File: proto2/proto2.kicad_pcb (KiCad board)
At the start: 2 copper layers, 166 x 111 mm, 158 parts, among them J1 Output 1, J10 Output 6, J11 Device 4, J2 Main Power, J3 Output 2, J4 Output 3, J5 Device 4, J6 Output 4, J7 Device 4, J8 Output 5, J9 Device 4, SW1 SW_DIP_x04, U1 AQY282SX, U10 AQY282SX, U11 AQY282SX, U12 AQY282SX, U13 AP1117-50, U14 JTD1548S15, U2 AQY282SX, U3 AQY282SX, U4 AQY282SX, U5 AQY282SX, U6 AQY282SX, U7 AQY282SX, U8 AQY282SX, U9 AQY282SX

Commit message: Routed Board.
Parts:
- removed U14: JTD1548S15, Converter_DCDC:Converter_DCDC_XP_POWER_JTDxxxxxxx_THT
- added C43: 1nF 2kV, Capacitor_SMD:C_0805_2012Metric, F.Cu at (192.8, 106.4)
- added C44: 330uF, Capacitor_SMD:C_0805_2012Metric, F.Cu at (198.8, 128.0)
- added C45: 4.7uF, Capacitor_SMD:C_0805_2012Metric, F.Cu at (198.8, 123.2)
- added C46: 4.7uF, Capacitor_SMD:C_0805_2012Metric, F.Cu at (198.8, 109.2)
- added C47: 330uF, Capacitor_SMD:C_0805_2012Metric, F.Cu at (198.8, 113.2)
- added C48: 100uF, Capacitor_SMD:C_0805_2012Metric, F.Cu at (173.5, 83.2)
- added C49: 1nF 2kV, Capacitor_SMD:C_0805_2012Metric, F.Cu at (192.8, 78.8)
- added C50: 0.33uF, Capacitor_SMD:C_0805_2012Metric, F.Cu at (163.3, 80.3)
- added C51: 01.uF, Capacitor_SMD:C_0805_2012Metric, F.Cu at (160.6, 73.1)
- added C52: 0.1uF, Capacitor_SMD:C_1206_3216Metric, F.Cu at (37.0, 142.5)
- added C53: 0.1uF, Capacitor_SMD:C_1206_3216Metric, F.Cu at (211.8, 141.8)
- added F13: 1A, Resistor_SMD:R_1206_3216Metric, F.Cu at (197.8, 133.5)
- added F14: 500mA, Resistor_SMD:R_0805_2012Metric, F.Cu at (43.8, 139.2)
- added F15: 500mA, Resistor_SMD:R_0805_2012Metric, F.Cu at (61.2, 139.2)
- added F16: 500mA, Resistor_SMD:R_0805_2012Metric, F.Cu at (78.8, 139.2)
- added F17: 500mA, Resistor_SMD:R_0805_2012Metric, F.Cu at (96.2, 139.2)
- added J12: Daughter Card, Connector_PinHeader_2.54mm:PinHeader_1x10_P2.54mm_Vertical, F.Cu at (156.4, 58.0)
- added L43: 2.2uH, Inductor_BCR:Murata_LQH32PN2R2NN0L, F.Cu at (197.8, 117.8)
- added PS1: CUI PDQE20, Converter_BCR:CUI_PDQE20, F.Cu at (187.5, 92.5)
- added R19: R Trim Up, Capacitor_SMD:C_0805_2012Metric, F.Cu at (172.8, 88.5)
- added R20: R Trim Down, Capacitor_SMD:C_0805_2012Metric, F.Cu at (172.5, 95.5)
- added R21: 0R, Capacitor_SMD:C_1206_3216Metric, F.Cu at (159.6, 76.6)
- added REF**: NPTH-.125, STD-xxx:NPTH-.125, F.Cu at (165.0, 103.0)
- added REF**: NPTH-.125, STD-xxx:NPTH-.125, F.Cu at (125.0, 103.0)
- added REF**: Langhe_Carrot, BCR_Art:Langhe_Carrot, F.Cu at (202.4, 70.0)
- MH1, MH3: footprint BCR_STD:STD-M6 -> STD-xxx:NPTH-.125
- MH2, MH4: footprint BCR_STD:STD-M6 -> STD-xxx:STD-.125_wide
- R17, R18: value 1M -> 0R
- SW1: footprint Package_SO:SOP-8_6.62x9.15mm_P2.54mm -> Button_Switch_BCR:CUI_DS04-254-2-04BK-SMT
- U13: value AP1117-50 -> LDO
- moved MH2 137.4 mm to (35.2, 158.0)
- moved R18 137.1 mm to (215.2, 141.8)
- moved MH4 116.1 mm to (213.2, 158.0)
- moved R17 115.6 mm to (33.2, 142.5)
- moved MH1 105.8 mm to (35.2, 58.0)
- moved C18 105.6 mm to (43.8, 143.2), turned to 270 degrees
- moved C16 101.8 mm to (50.8, 143.2), turned to 270 degrees
- moved C17 97.4 mm to (47.2, 143.2), turned to 270 degrees
- moved C26 95.2 mm to (61.2, 143.2), turned to 270 degrees
- moved C15 93.6 mm to (54.2, 143.2), turned to 270 degrees
- moved C23 89.4 mm to (71.8, 143.2), turned to 270 degrees
- moved C25 87.2 mm to (64.8, 143.2), turned to 270 degrees
- moved C31 80.7 mm to (89.2, 143.2), turned to 270 degrees
- moved C38 79.4 mm to (191.5, 137.0), turned to 180 degrees
- moved C24 79.3 mm to (68.2, 143.2), turned to 270 degrees
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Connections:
- net VDQ renamed VDQ1
- BB1 pad 8.13: Net-(BB1-Pad8.13) -> OUT_1
- BB1 pad 8.15: Net-(BB1-Pad8.15) -> OUT_2
- BB1 pad 8.17: Net-(BB1-Pad8.17) -> OUT_3
- BB1 pad 8.19: Net-(BB1-Pad8.19) -> OUT_4
- BB1 pad 8.20: OUT_1 -> Net-(BB1-Pad8.20)
- BB1 pad 8.21: Net-(BB1-Pad8.21) -> OUT_5
- BB1 pad 8.22: OUT_2 -> Net-(BB1-Pad8.22)
- BB1 pad 8.23: Net-(BB1-Pad8.23) -> OUT_6
- BB1 pad 8.24: OUT_3 -> Net-(BB1-Pad8.24)
- BB1 pad 8.25: Net-(BB1-Pad8.25) -> OUT_7
- BB1 pad 8.26: OUT_4 -> Net-(BB1-Pad8.26)
- BB1 pad 8.27: Net-(BB1-Pad8.27) -> OUT_8
- BB1 pad 8.28: OUT_5 -> Net-(BB1-Pad8.28)
- BB1 pad 8.29: Net-(BB1-Pad8.29) -> OUT_9
- BB1 pad 8.30: OUT_6 -> Net-(BB1-Pad8.30)
- BB1 pad 8.31: Net-(BB1-Pad8.31) -> OUT_10
- BB1 pad 8.32: OUT_7 -> Net-(BB1-Pad8.32)
- BB1 pad 8.33: Net-(BB1-Pad8.33) -> OUT_11
- BB1 pad 8.34: OUT_8 -> Net-(BB1-Pad8.34)
- BB1 pad 8.35: Net-(BB1-Pad8.35) -> OUT_12
- BB1 pad 8.36: OUT_9 -> GP_4
- BB1 pad 8.40: OUT_10 -> GP_3
- BB1 pad 8.42: Net-(BB1-Pad8.42) -> GP_2
- BB1 pad 8.44: OUT_11 -> GP_1
- BB1 pad 8.46: OUT_12 -> BS_5
- C18 pad 1: +5V -> 5V_1
- C26 pad 1: +5V -> 5V_2
- C34 pad 1: +5V -> 5V_3
- C42 pad 1: +5V -> 5V_4
- D1 pad 2: Earth -> Net-(D1-Pad2)
- D10 pad 2: Earth -> Net-(D10-Pad2)
- D11 pad 2: Earth -> Net-(D11-Pad2)
- D12 pad 2: Earth -> Net-(D12-Pad2)
- D2 pad 2: Earth -> Net-(D2-Pad2)
- D3 pad 2: Earth -> Net-(D3-Pad2)
- D4 pad 2: Earth -> Net-(D4-Pad2)
- D5 pad 2: Earth -> Net-(D5-Pad2)
- D6 pad 2: Earth -> Net-(D6-Pad2)
- D7 pad 2: Earth -> Net-(D7-Pad2)
- D8 pad 2: Earth -> Net-(D8-Pad2)
- D9 pad 2: Earth -> Net-(D9-Pad2)
- F2 pad 1: DQ01_2 -> DQ1_2
- J1 pad 2: Net-(J1-Pad2) -> Net-(D1-Pad2)
- J1 pad 4: Net-(J1-Pad4) -> Net-(D2-Pad2)
- J10 pad 2: Net-(J10-Pad2) -> Net-(D11-Pad2)
- J10 pad 3: Net-(J10-Pad3) -> Net-(D12-Pad1)
- J10 pad 4: Net-(J10-Pad3) -> Net-(D12-Pad2)
- J3 pad 2: Net-(J3-Pad2) -> Net-(D3-Pad2)
- J3 pad 4: Net-(J3-Pad4) -> Net-(D4-Pad2)
- J4 pad 2: Net-(J4-Pad2) -> Net-(D5-Pad2)
- J4 pad 4: Net-(J4-Pad4) -> Net-(D6-Pad2)
- J6 pad 2: Net-(J6-Pad2) -> Net-(D7-Pad2)
- J6 pad 4: Net-(J6-Pad4) -> Net-(D8-Pad2)
- J8 pad 2: Net-(J8-Pad2) -> Net-(D9-Pad2)
- J8 pad 4: Net-(J8-Pad4) -> Net-(D10-Pad2)
- L10 pad 2: Net-(J3-Pad4) -> Net-(D4-Pad2)
- L12 pad 2: Net-(J4-Pad2) -> Net-(D5-Pad2)
- L14 pad 1: +5V -> 5V_1
- L15 pad 2: Net-(J4-Pad4) -> Net-(D6-Pad2)
- L2 pad 2: Net-(J1-Pad2) -> Net-(D1-Pad2)
- L20 pad 2: Net-(J6-Pad2) -> Net-(D7-Pad2)
- L22 pad 2: Net-(J6-Pad4) -> Net-(D8-Pad2)
- L23 pad 1: +5V -> 5V_2
- L28 pad 2: Net-(J8-Pad2) -> Net-(D9-Pad2)
- L30 pad 2: Net-(J8-Pad4) -> Net-(D10-Pad2)
- L31 pad 1: +5V -> 5V_3
- L36 pad 2: Net-(J10-Pad2) -> Net-(D11-Pad2)
- L37 pad 2: Net-(J10-Pad3) -> Net-(D12-Pad1)
- L38 pad 2: Net-(J10-Pad3) -> Net-(D12-Pad2)
- L39 pad 1: +5V -> 5V_4
- L4 pad 2: Net-(J1-Pad4) -> Net-(D2-Pad2)
- L8 pad 2: Net-(J3-Pad2) -> Net-(D3-Pad2)
- R10 pad 2: OUT_10 -> OUT_6
- R11 pad 2: OUT_3 -> OUT_7
- R12 pad 2: OUT_7 -> OUT_8
- R13 pad 2: OUT_11 -> OUT_9
- R14 pad 2: OUT_4 -> OUT_10
- R15 pad 2: OUT_8 -> OUT_11
- R6 pad 2: OUT_5 -> OUT_2
- R7 pad 2: OUT_9 -> OUT_3
- R8 pad 2: OUT_2 -> OUT_4
- R9 pad 2: OUT_6 -> OUT_5
- RP1 pad 11: OUT_3 -> BS_3
- RP1 pad 13: OUT_2 -> BS_2
- RP1 pad 15: OUT_1 -> BS_1
- RP1 pad 24: Net-(RP1-Pad24) -> BS_5
- RP1 pad 29: Net-(RP1-Pad29) -> OUT_4
- RP1 pad 31: BS_1 -> OUT_3
- RP1 pad 33: BS_2 -> OUT_2
- RP1 pad 35: BS_3 -> OUT_1
- RP1 pad 37: BS_4 -> Net-(RP1-Pad37)
- RP1 pad 7: OUT_4 -> BS_4
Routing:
- net +5V: track 0.00 -> 321.4 mm, vias 0 -> 4
- net OUT_12: track 0.00 -> 241.1 mm, vias 0 -> 5
- net OUT_11: track 0.00 -> 232.3 mm, vias 0 -> 5
- net OUT_10: track 0.00 -> 223.0 mm, vias 0 -> 5
- net OUT_9: track 0.00 -> 212.0 mm, vias 0 -> 5
- net OUT_4: track 0.00 -> 204.1 mm, vias 0 -> 4
- net OUT_8: track 0.00 -> 202.0 mm, vias 0 -> 5
- net OUT_3: track 0.00 -> 191.3 mm, vias 0 -> 4
- net OUT_7: track 0.00 -> 190.6 mm, vias 0 -> 5
- net BS_5: track 0.00 -> 185.0 mm, vias 0 -> 4
- net OUT_6: track 0.00 -> 182.0 mm, vias 0 -> 5
- net OUT_2: track 0.00 -> 179.6 mm, vias 0 -> 4
- net OUT_1: track 0.00 -> 172.5 mm, vias 0 -> 4
- net OUT_5: track 0.00 -> 170.6 mm, vias 0 -> 5
- net BS_1: track 0.00 -> 146.0 mm, vias 0 -> 3
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- added copper zone on B.Cu, net Earth
- added copper zone on B.Cu, net GND
- added copper zone on F.Cu, net GNDPWR
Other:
- board size 166 x 111 mm -> 187.5 x 109.8 mm
- board text added: "Langhe Greenhaus ©2021 LNG-PCB-003"

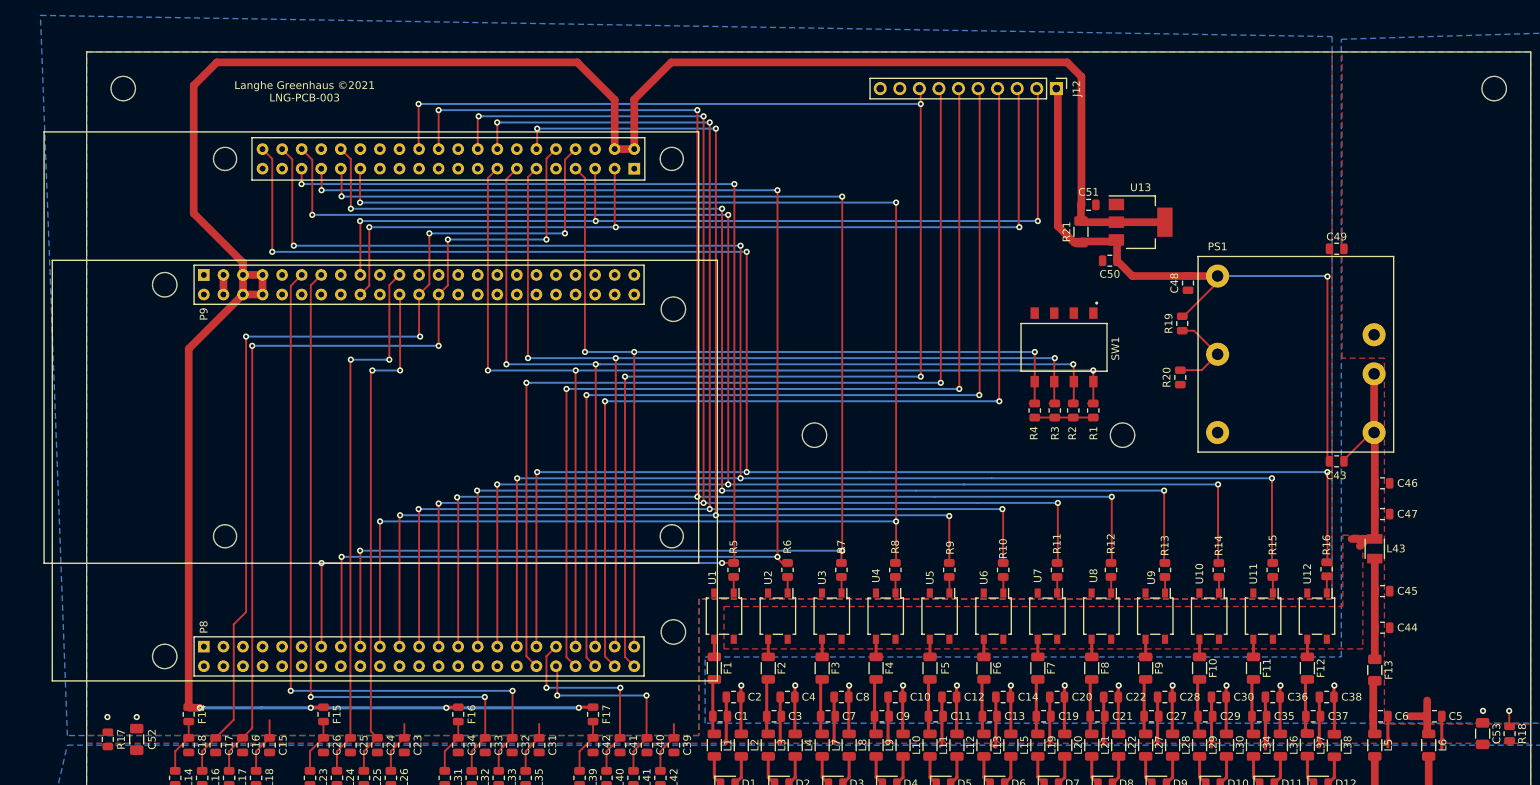
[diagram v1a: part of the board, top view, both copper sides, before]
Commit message: Added correct cap and moved DIP switches.
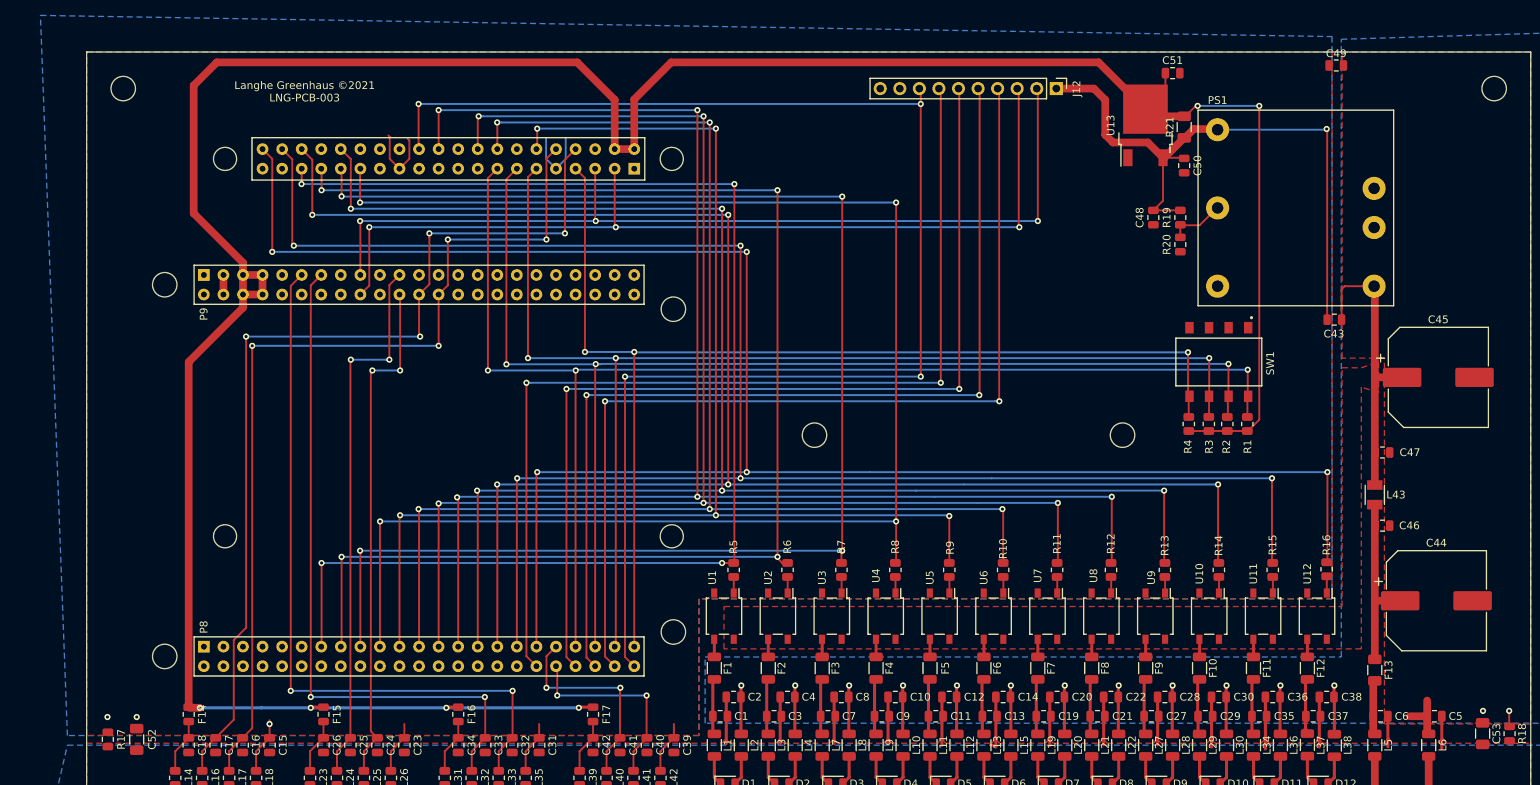
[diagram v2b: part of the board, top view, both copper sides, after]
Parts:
- C44: footprint Capacitor_SMD:C_0805_2012Metric -> Capacitor_BCR:CP_Elec_13x12.5
- C45: value 4.7uF -> 330uF; footprint Capacitor_SMD:C_0805_2012Metric -> Capacitor_BCR:CP_Elec_13x12.5
- C47: value 330uF -> 4.7uF
- U13: footprint Package_TO_SOT_SMD:SOT-223-3_TabPin2 -> JLCPCB:TO-252-2
- moved C45 28.7 mm to (206.0, 95.5)
- moved C49 23.8 mm to (192.8, 55.0)
- moved C51 20.3 mm to (171.5, 56.0)
- moved SW1 20.2 mm to (177.5, 93.5)
- moved R1 20.1 mm to (181.2, 101.5)
- moved R2 20.1 mm to (178.6, 101.5)
- moved R3 20.1 mm to (176.2, 101.5)
- moved R4 20.1 mm to (173.6, 101.5)
- moved R21 19.1 mm to (173.0, 63.0)
- moved PS1 19.0 mm to (187.5, 73.5)
- moved C43 18.4 mm to (192.5, 88.0)
- moved R20 17.2 mm to (172.5, 78.2)
- moved C50 15.7 mm to (173.0, 68.0), turned to 270 degrees
- moved R19 13.8 mm to (172.5, 74.8)
- moved U13 12.6 mm to (168.0, 62.8), turned to 90 degrees
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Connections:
- C45 pad 1: Net-(C44-Pad1) -> VDQ1
- C46 pad 1: VDQ1 -> Net-(C44-Pad1)
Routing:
- net +5V: track 321.4 -> 369.2 mm, vias 4 -> 6
- net BS_1: track 146.0 -> 167.4 mm
- net BS_3: track 137.6 -> 158.8 mm
- net BS_4: track 128.2 -> 149.3 mm
- net BS_2: track 142.5 -> 163.5 mm
- net GND: track 27.7 -> 46.0 mm, vias 2 -> 3
- net Net-(C44-Pad1): track 13.1 -> 22.1 mm
- net VDD: track 88.3 -> 81.7 mm
- net /Power/TRIM: track 11.6 -> 7.42 mm
- net VDQ1: track 32.7 -> 36.3 mm

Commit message: Finished routing board and other changes, bad commit message, I know.
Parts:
- C43, C46, C47, C49: footprint Capacitor_SMD:C_0805_2012Metric -> Capacitor_SMD:C_1206_3216Metric
- C51: value 01.uF -> 0.1uF
- C52, C53: footprint Capacitor_SMD:C_1206_3216Metric -> Capacitor_SMD:C_0805_2012Metric
- D1, D10, D11, D12, D2, D3, D4, D5, D6, D7, D8, D9: footprint Diode_SMD:D_0805_2012Metric -> Diode_SMD:D_SOD-123F
- J10: value Output 6 -> Output
- J11, J5, J7, J9: value Device 4 -> Device
- J3: value Output 2 -> Output
- J4: value Output 3 -> Output
- J6: value Output 4 -> Output
- J8: value Output 5 -> Output
- L1, L10, L11, L12, L13, L15, L19, L2, L20, L21, L22, L27, L28, L29, L3, L30, L34, L36, L37, L38, L4, L7, L8, L9: value Ferrite_Bead_Small -> 1A Ferrite
- L14, L16, L17, L18, L23, L24, L25, L26, L31, L32, L33, L35, L39, L40, L41, L42: value Ferrite_Bead_Small -> 500mA Ferrite
- L43: value 2.2uH -> 2.2uH 1.6A
- L5, L6: value 100R 5A -> 100R 5A Ferrite; footprint Resistor_SMD:R_1206_3216Metric -> Inductor_BCR:Coilmax_MS0630-2R2M
- moved C5 5.94 mm to (211.0, 141.8), turned to 270 degrees
- moved C53 4.50 mm to (216.2, 141.8)
- moved C6 4.16 mm to (195.0, 141.8), turned to 270 degrees
- moved L5 2.30 mm to (199.5, 141.8)
- moved L6 2.30 mm to (206.5, 141.8)
- moved C46 1.75 mm to (200.5, 114.8)
- moved C47 1.75 mm to (200.5, 105.2)
- moved R18 1.50 mm to (213.8, 141.8)
- moved C43 0.25 mm to (192.8, 88.0)
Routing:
- net VDQ1: track 36.3 -> 42.8 mm
- net VIN: track 7.05 -> 10.2 mm
- net Earth: track 84.8 -> 82.7 mm, vias 14 -> 12
- net Net-(C44-Pad1): track 22.1 -> 23.5 mm
- net GNDPWR: track 87.2 -> 86.2 mm
